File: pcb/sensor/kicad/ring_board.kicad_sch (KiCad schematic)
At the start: 11 parts, among them J1 5V in (FFC), J2 CN2 mate (TBD), J3 mic carrier, U1 SHT45

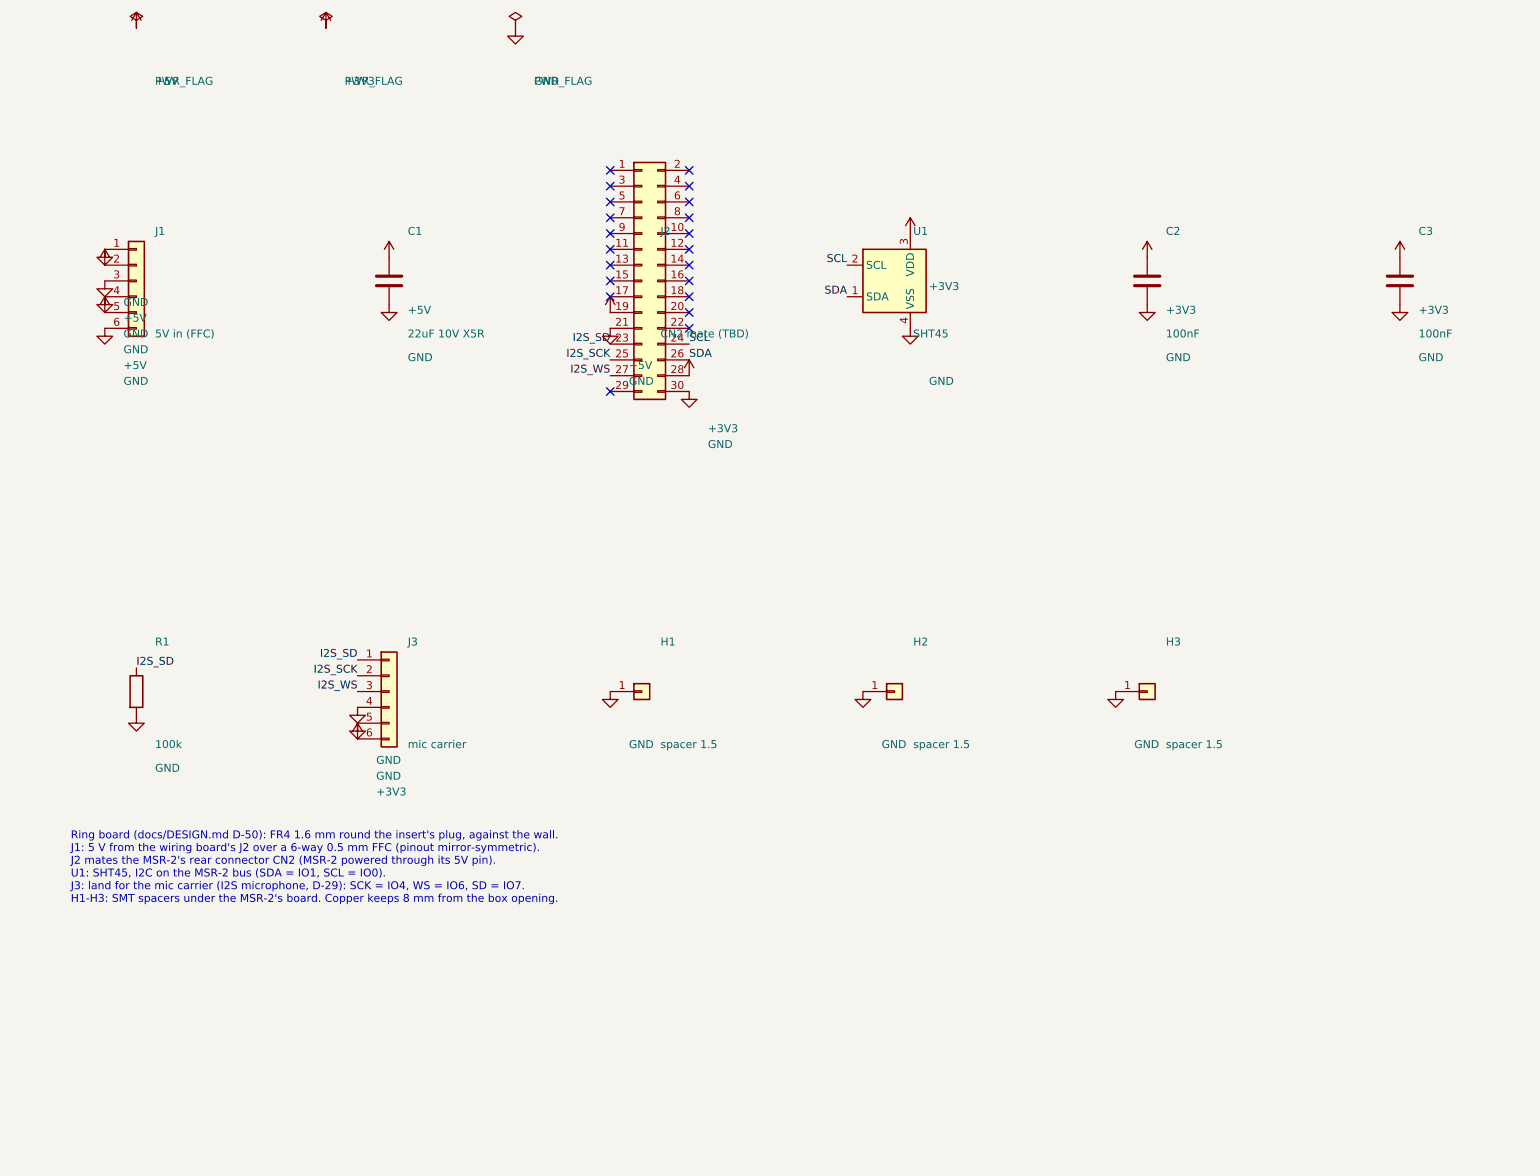
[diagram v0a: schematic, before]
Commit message: Mic on the boards, parts audit, rocker second source, CN2 land pattern, back cover fit (D-82..D-90)
- Prototype PCBWay packs for the ring board, EU cap board and cover flex; logos and URL on the
  boards with room for them
- CN2 mate: Molex 55909-2474 on an assumed 51338-2474 (D-82); land pattern from Molex
  SD-55909-003 rev J, B2B from SD-51338-003 rev K (D-89); contact map and pin 1 still open
- Microphone: Knowles SPK0641HT4H-1 + ADAU7002 on the ring board and the EU cap board, the mic
  carrier removed; face plate sound column on a gasket (D-83); C3 KEMET C1206C104J3GACTU C0G
  (D-85)
- Parts rule (active, stocked at DigiKey or Mouser) and audit: F1 3403.0166.11, cover flex 1 uF
  CL05A105KO5NNNC, rocker at Mouser 979-1802.2504 (D-84)
- Rocker: tabs soldered into plated slots accepted (D-86); E-Switch RA412C1100 second source,
  slotted footprint on the wiring board and the EU mains board, solder the rocker after the
  board is screwed down (D-88)
- Back cover: round-over 8.1 x 8.0 from the printed gauges (D-87); four tabs inside the long
  side walls into the housing's slots (D-90); back_gauges_PLA
- make stock / make order-push (pcb/tools/distributors.py): live DigiKey / Mouser stock and
  lifecycle, DigiKey myLists link and Mouser cart; keys from the environment only
- Boards ERC / DRC clean; make check, make eu, make check-renders pass; renders, fab and
  order packs regenerated
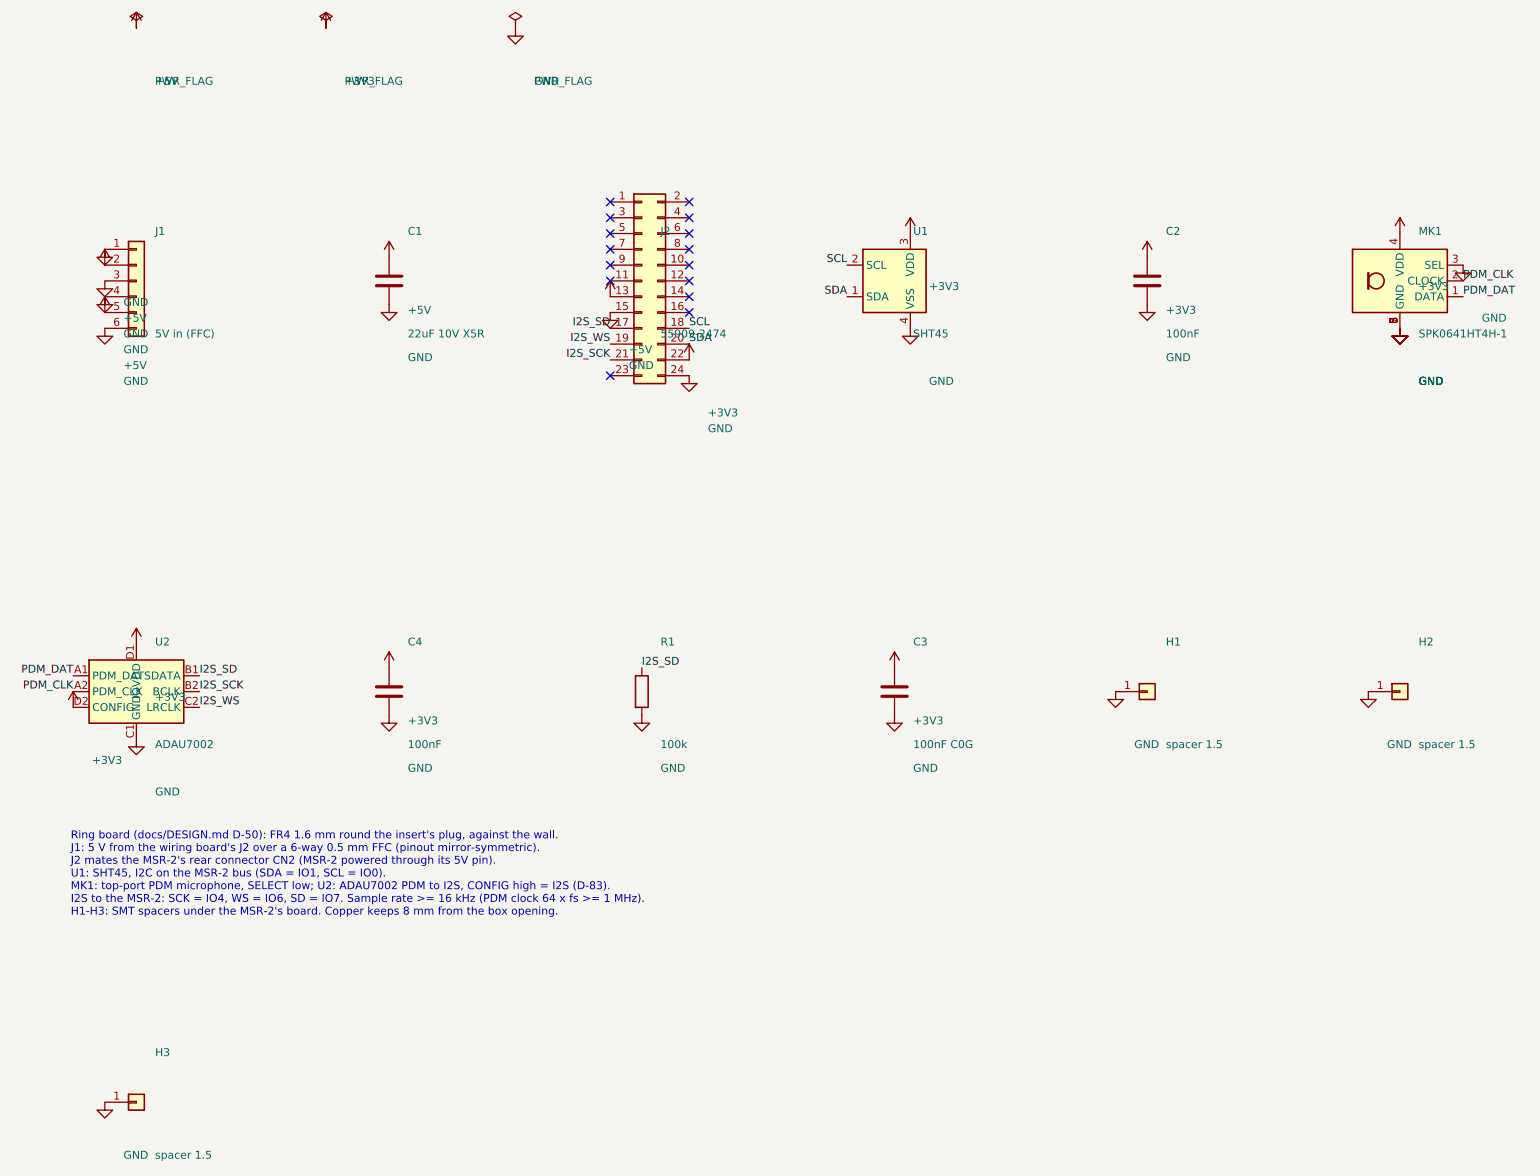
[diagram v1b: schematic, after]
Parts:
- removed J3: mic carrier, sensor:Mic_Carrier_Land_2x3, symbol sensor:Conn_01x06
- added C4: 100nF, sensor:C_0402_1005Metric, symbol sensor:C
- added MK1: SPK0641HT4H-1, sensor:Knowles_SPK0641HT4H-1_3x4mm, symbol sensor:SPK0641HT4H-1
- added U2: ADAU7002, sensor:Analog_WLCSP-8_0.76x1.56mm_P0.4mm, symbol sensor:ADAU7002
- C3: value 100nF -> 100nF C0G; footprint sensor:C_0402_1005Metric -> sensor:C_1206_3216Metric; MPN 0402 X7R 100 nF 16 V -> C1206C104J3GACTU; Manufacturer any -> KEMET
- J2: value CN2 mate (TBD) -> 55909-2474; footprint sensor:B2B_0.4mm_2x15_PLACEHOLDER -> sensor:Molex_SlimStack_55909-2474_2x12_P0.40mm_Vertical; symbol sensor:Conn_02x15_Odd_Even -> sensor:Conn_02x12_Odd_Even; MPN TBD -> 55909-2474; Manufacturer TBD -> Molex
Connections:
- net +3V3: now also J2.22 (Pin_22), C4.1, MK1.4 (VDD), U2.D1 (IOVDD), U2.D2 (CONFIG); no longer J2.28 (Pin_28)
- net +5V: now also J2.13 (Pin_13); no longer J2.19 (Pin_19)
- net GND: now also J2.15 (Pin_15), J2.24 (Pin_24), C4.2, MK1.3 (SEL), MK1.5 (GND), MK1.6 (GND), MK1.7 (GND), MK1.8 (GND), U2.C1 (GND); no longer J2.21 (Pin_21), J2.30 (Pin_30)
- net I2S_SCK: now also J2.21 (Pin_21), U2.B2 (BCLK); no longer J2.25 (Pin_25)
- net I2S_SD: now also J2.17 (Pin_17), U2.B1 (SDATA); no longer J2.23 (Pin_23)
- net I2S_WS: now also J2.19 (Pin_19), U2.C2 (LRCLK); no longer J2.27 (Pin_27)
- net SCL: now also J2.18 (Pin_18); no longer J2.24 (Pin_24)
- net SDA: now also J2.20 (Pin_20); no longer J2.26 (Pin_26)
- new net PDM_CLK: MK1.2 (CLOCK), U2.A2 (PDM_CLK)
- new net PDM_DAT: MK1.1 (DATA), U2.A1 (PDM_DAT)
- no-connect marks 21 -> 15
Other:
- note added: "Ring board (docs/DESIGN.md D-50): FR4 1.6 mm round the insert's plug, against the wall. J1: 5 V from the wiring board's J2 over a 6-way 0.5 mm FFC (pinout mirror-symmetric). J2 mates the MSR-2's rear connector CN2 (MSR-2 powered through its 5V pin). U1: SHT45, I2C on the MSR-2 bus (SDA = IO1, SCL = IO0). MK1: top-port PDM microphone, SELECT low; U2: ADAU7002 PDM to I2S, CONFIG high = I2S (D-83). 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"
- note removed: "Ring board (docs/DESIGN.md D-50): FR4 1.6 mm round the insert's plug, against the wall. J1: 5 V from the wiring board's J2 over a 6-way 0.5 mm FFC (pinout mirror-symmetric). J2 mates the MSR-2's rear connector CN2 (MSR-2 powered through its 5V pin). U1: SHT45, I2C on the MSR-2 bus (SDA = IO1, SCL = IO0). J3: land for the mic carrier (I2S microphone, D-29): SCK = IO4, WS = IO6, SD = IO7. H1-H3: SM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"
- moved on the sheet: C3, H1, H2, H3, R1

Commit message: Parts and order lists: EU PE connector, 22 uF C1, unit and devkit lists, E-Switch rocker (D-94, D-95, D-97)
- D-94: the EU lights' PE joined in the box in a WAGO 221-412 (EXTRA_EU, ASSEMBLY step 5); the
  boards carry no PE; the steel piece's insulation added to the EU review checklist
- D-95: 22 uF C1 KEMET C1206C226M4PACTU (16 V X5R, 1.8 max) on the ring board, the EU cap board
  and the EU 5 V board; the Samsung CL31A226KPHNNNE has a 61-week maker lead time
- D-97: make order writes unit_na, unit_eu, devkit_na, devkit_eu (4 sets per variant,
  DEVKIT_SETS), exact counts; the PCBWay packs are the devkit (5 PCBs per design); the old
  3 NA + 2 EU lists removed
- Rocker: both variants' lists take the E-Switch RA412C1100 (RA4 datasheet rating option C:
  UL/cUL 10 A 250 VAC; ENEC 10(4) A 250 V~); the Marquardt stays the reference part
- ADAU7002 to DigiKey in Mouser orders (Mouser does not restock it); stale PCBWay notes fixed
- Boards ERC / DRC clean; renders regenerated
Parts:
- C1: value 22uF 10V X5R -> 22uF 16V X5R; MPN CL31A226KPHNNNE -> C1206C226M4PACTU; Manufacturer Samsung Electro-Mechanics -> KEMET
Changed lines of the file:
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@@
 			)
 		)
-		(property "Value" "22uF 10V X5R"
+		(property "Value" "22uF 16V X5R"
 			(at 79.2 99.94 0)
 			(effects
@@
 			)
 		)
-		(property "Datasheet" "https://www.samsungsem.com"
+		(property "Datasheet" "https://yageogroup.com/content/datasheet/asset/file/KEM_C1006_X5R_SMD"
 			(at 76.2 91.44 0)
 			(effects
@@
 			)
 		)
-		(property "Description" "Ceramic 22 uF 10 V X5R 1206 at J1"
+		(property "Description" "Ceramic 22 uF 16 V X5R 1206 at J1, 1.8 mm max"
 			(at 76.2 91.44 0)
 			(effects
@@
 			)
 		)
-		(property "Manufacturer" "Samsung Electro-Mechanics"
+		(property "Manufacturer" "KEMET"
 			(at 76.2 91.44 0)
 			(effects
@@
 			)
 		)
-		(property "MPN" "CL31A226KPHNNNE"
+		(property "MPN" "C1206C226M4PACTU"
 			(at 76.2 91.44 0)
 			(effects

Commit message: Cost: SHT40, Murata C0G, GCT FFC (D-98)
- U1 SHT45-AD1B-R2 -> SHT40-AD1B-R2 (same SHT4x DFN-4, I2C 0x44; 9.76 -> 3.10 CAD); renamed in
  the CAD, generators and docs
- C3 KEMET C1206C104J3GACTU -> Murata GRM3195C1H104JA05D (100 nF C0G 50 V 1206, 0.95 max;
  3.52 -> 0.58)
- W1 FFC Wurth 687606152002 -> GCT 05-06-A-0152-A-4-06-4-G (same cable; 4.67 -> 3.26), the
  Wurth as the alternative
- DigiKey, one plate: NA 90.04 -> 79.03, EU 88.51 -> 78.91 CAD; boards ERC / DRC clean, order
  lists and PCBWay packs regenerated
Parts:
- C3: MPN C1206C104J3GACTU -> GRM3195C1H104JA05D; Manufacturer KEMET -> Murata
- U1: value SHT45 -> SHT40; MPN SHT45-AD1B-R2 -> SHT40-AD1B-R2
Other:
- note added: "Ring board (docs/DESIGN.md D-50): FR4 1.6 mm round the insert's plug, against the wall. J1: 5 V from the wiring board's J2 over a 6-way 0.5 mm FFC (pinout mirror-symmetric). J2 mates the MSR-2's rear connector CN2 (MSR-2 powered through its 5V pin). U1: SHT40, I2C on the MSR-2 bus (SDA = IO1, SCL = IO0). MK1: top-port PDM microphone, SELECT low; U2: ADAU7002 PDM to I2S, CONFIG high = I2S (D-83). 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"
- note removed: "Ring board (docs/DESIGN.md D-50): FR4 1.6 mm round the insert's plug, against the wall. J1: 5 V from the wiring board's J2 over a 6-way 0.5 mm FFC (pinout mirror-symmetric). J2 mates the MSR-2's rear connector CN2 (MSR-2 powered through its 5V pin). U1: SHT45, I2C on the MSR-2 bus (SDA = IO1, SCL = IO0). MK1: top-port PDM microphone, SELECT low; U2: ADAU7002 PDM to I2S, CONFIG high = I2S (D-83). 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"
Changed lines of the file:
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@@
 			)
 		)
-		(property "Value" "SHT45"
+		(property "Value" "SHT40"
 			(at 160.48 99.94 0)
 			(effects
@@
 			)
 		)
-		(property "MPN" "SHT45-AD1B-R2"
+		(property "MPN" "SHT40-AD1B-R2"
 			(at 157.48 91.44 0)
 			(effects
@@
 			)
 		)
-		(property "Description" "SHT45 decoupling"
+		(property "Description" "SHT40 decoupling"
 			(at 198.12 91.44 0)
 			(effects
@@
 			)
 		)
-		(property "Datasheet" "https://content.kemet.com/datasheets/KEM_C1003_C0G_SMD.pdf"
+		(property "Datasheet" "https://pim.murata.com/asset/pim4/ceramicCapacitorSMD/GRM3195C1H104JA05-01A-EN_PDF_CERAMICCAPACITORSMD"
 			(at 157.48 157.48 0)
 			(effects
@@
 			)
 		)
-		(property "Description" "Microphone decoupling, C0G 25 V 1206"
+		(property "Description" "Microphone decoupling, C0G 50 V 1206"
 			(at 157.48 157.48 0)
 			(effects
@@
 			)
 		)
-		(property "Manufacturer" "KEMET"
+		(property "Manufacturer" "Murata"
 			(at 157.48 157.48 0)
 			(effects
@@
 			)
 		)
-		(property "MPN" "C1206C104J3GACTU"
+		(property "MPN" "GRM3195C1H104JA05D"
 			(at 157.48 157.48 0)
 			(effects
@@
 		)
 	)
-	(text "Ring board (docs/DESIGN.md D-50): FR4 1.6 mm round the insert's plug, against the wall.\nJ1: 5 V from the wiring board's J2 over a 6-way 0.5 mm FFC (pinout mirror-symmetric).\nJ2 mates the MSR-2's rear connector CN2 (MSR-2 powered through its 5V pin).\nU1: SHT45, I2C on the MSR-2 bus (SDA = IO1, SCL = IO0).\nMK1: top-port PDM microphone, SELECT low; U2: ADAU7002 PDM to I2S, CONFIG high = I2S (D-83).\nI2S to the MSR-2: SCK = IO4, WS = IO6, SD = IO7. Sample rate >= 16 kHz (PDM clock 64 x fs >= 1 MHz).\nH1-H3: SMT spacers under the MSR-2's board. Copper keeps 8 mm from the box opening."
+	(text "Ring board (docs/DESIGN.md D-50): FR4 1.6 mm round the insert's plug, against the wall.\nJ1: 5 V from the wiring board's J2 over a 6-way 0.5 mm FFC (pinout mirror-symmetric).\nJ2 mates the MSR-2's rear connector CN2 (MSR-2 powered through its 5V pin).\nU1: SHT40, I2C on the MSR-2 bus (SDA = IO1, SCL = IO0).\nMK1: top-port PDM microphone, SELECT low; U2: ADAU7002 PDM to I2S, CONFIG high = I2S (D-83).\nI2S to the MSR-2: SCK = IO4, WS = IO6, SD = IO7. Sample rate >= 16 kHz (PDM clock 64 x fs >= 1 MHz).\nH1-H3: SMT spacers under the MSR-2's board. Copper keeps 8 mm from the box opening."
 		(exclude_from_sim no)
 		(at 25 180 0)

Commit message: Flex review fixes, back cover clip, README, Sladdseg, order lists (D-116..D-119)
- D-116: cover flex: 0603 X5R input/output caps, ESD diode TPD1E10B06DYAR,
  0.6 mm bend radius with relief slits, stiffener notch and outlines,
  coverlay expansion, mask-defined pin pads, teardrops, fab notes; the
  cover's snap hooks allow for stiffener adhesive and tolerance
- D-117, D-118: bottom clip catch 3.22 above the floor, tip as far proud of
  the shell as the top clip's
- Battery polarity confirmed on a unit
- README rewritten: three editions, assembly renders, safety and polarity
  warnings, cost for 1 to 10,000 plates, printed parts; detail and board
  renders moved to their docs; the product is named Sladdseg
- EU boards: the ant logo on the other face
- D-119: order lists: one NA plate, one EU plate, a devkit of 5 + 5
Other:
- title: Smart wall plate - ring board -> Sladdseg - ring board
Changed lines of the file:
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@@
 	(paper "A4")
 	(title_block
-		(title "Smart wall plate - ring board")
+		(title "Sladdseg - ring board")
 		(date "2026-10-12")
 		(rev "v0.5")
